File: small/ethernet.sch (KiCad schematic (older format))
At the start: 26 parts, among them J6 RJ45_Amphenol_RJMG1BD3B8K1ANR, U4 ENC28J60x-SS, Y1 Crystal

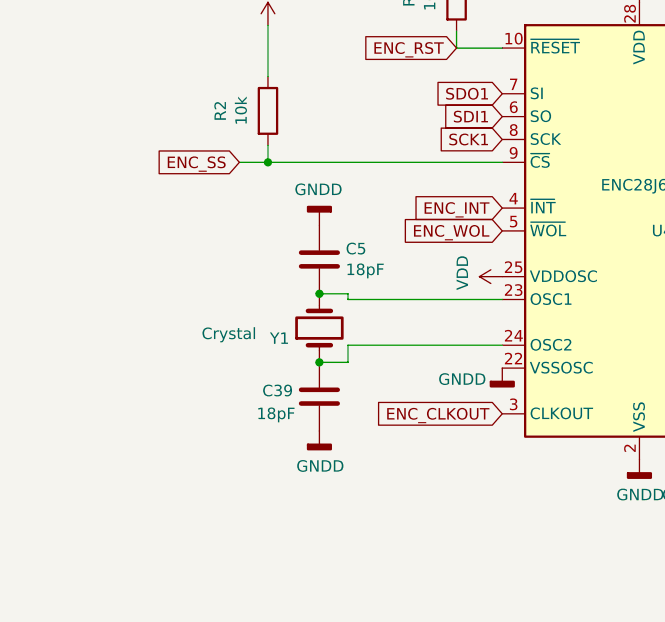
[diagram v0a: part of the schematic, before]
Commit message: oscillator footprint and capacitors changed
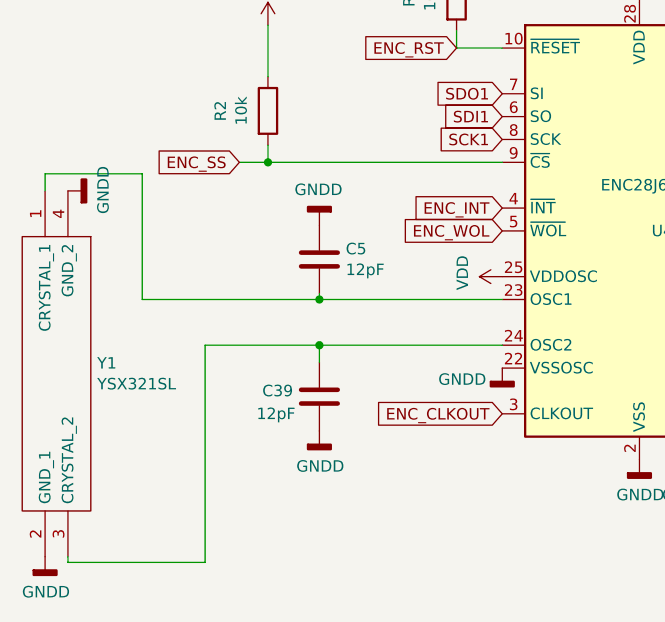
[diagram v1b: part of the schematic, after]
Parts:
- removed Y1: Crystal, Crystal:Crystal_SMD_3225-4Pin_3.2x2.5mm, symbol Device:Crystal
- added Y1: YSX321SL, small:YSX321SL, symbol YSX321SL:YSX321SL
- C39, C5: value 18pF -> 12pF; LCSC C1647 -> C38523; MPN CL10C180JB8NNNC -> CL10C120JB8NNNC
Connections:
- wire segments 76 -> 82
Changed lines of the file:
@@
 SDO1
-$Comp
-L Device:Crystal Y?
-U 1 1 60781A1A
-P 1850 3425
-AR Path="/60781A1A" Ref="Y?"  Part="1"
-AR Path="/60757620/60781A1A" Ref="Y1"  Part="1"
-F 0 "Y1" V 1804 3556 50  0000 L CNN
-F 1 "Crystal" V 1825 3700 50  0000 L CNN
-F 2 "Crystal:Crystal_SMD_3225-4Pin_3.2x2.5mm" H 1850 3425 50  0001 C CNN
-F 3 "https://datasheet.lcsc.com/szlcsc/Yangxing-Tech-X322525MOB4SI_C9006.pdf" H 1850 3425 50  0001 C CNN
-F 4 " C9006" V 1850 3425 50  0001 C CNN "LCSC"
-F 5 "X322525MOB4SI" H 1850 3425 50  0001 C CNN "MPN"
-F 6 "0" H 1850 3425 50  0001 C CNN "source"
-F 7 "0.0928" H 1850 3425 50  0001 C CNN "Price"
-	1    1850 3425
-	0    -1   -1   0
-$EndComp
-Wire Wire Line
-	2650 3300 1975 3300
-Wire Wire Line
-	1975 3300 1975 3275
-Wire Wire Line
-	1975 3275 1850 3275
-Wire Wire Line
-	2650 3500 1975 3500
-Wire Wire Line
-	1975 3500 1975 3575
-Wire Wire Line
-	1975 3575 1850 3575
 $Comp
 L Device:C C?
@@
 AR Path="/60757620/60781A26" Ref="C5"  Part="1"
 F 0 "C5" H 1965 3171 50  0000 L CNN
-F 1 "18pF" H 1965 3080 50  0000 L CNN
+F 1 "12pF" H 1965 3080 50  0000 L CNN
 F 2 "Capacitor_SMD:C_0603_1608Metric" H 1888 2975 50  0001 C CNN
-F 3 "https://datasheet.lcsc.com/szlcsc/Samsung-Electro-Mechanics-CL10C180JB8NNNC_C1647.pdf" H 1850 3125 50  0001 C CNN
-F 4 "C1647" H 1850 3125 50  0001 C CNN "LCSC"
-F 5 "CL10C180JB8NNNC" H 1850 3125 50  0001 C CNN "MPN"
+F 3 "https://datasheet.lcsc.com/szlcsc/Samsung-Electro-Mechanics-CL10C120JB8NNNC_C38523.pdf" H 1850 3125 50  0001 C CNN
+F 4 "C38523" H 1850 3125 50  0001 C CNN "LCSC"
+F 5 "CL10C120JB8NNNC" H 1850 3125 50  0001 C CNN "MPN"
 F 6 "0.0073" H 1850 3125 50  0001 C CNN "Price"
 F 7 "0" H 1850 3125 50  0001 C CNN "source"
@@
 	1    0    0    -1
 $EndComp
-Connection ~ 1850 3275
 $Comp
 L power:GNDD #PWR?
@@
 AR Path="/60757620/609672F4" Ref="C39"  Part="1"
 F 0 "C39" H 1600 3750 50  0000 L CNN
-F 1 "18pF" H 1575 3650 50  0000 L CNN
+F 1 "12pF" H 1575 3650 50  0000 L CNN
 F 2 "Capacitor_SMD:C_0603_1608Metric" H 1888 3575 50  0001 C CNN
-F 3 "https://datasheet.lcsc.com/szlcsc/Samsung-Electro-Mechanics-CL10C180JB8NNNC_C1647.pdf" H 1850 3725 50  0001 C CNN
-F 4 "C1647" H 1850 3725 50  0001 C CNN "LCSC"
-F 5 "CL10C180JB8NNNC" H 1850 3725 50  0001 C CNN "MPN"
+F 3 "https://datasheet.lcsc.com/szlcsc/Samsung-Electro-Mechanics-CL10C120JB8NNNC_C38523.pdf" H 1850 3725 50  0001 C CNN
+F 4 "C38523" H 1850 3725 50  0001 C CNN "LCSC"
+F 5 "CL10C120JB8NNNC" H 1850 3725 50  0001 C CNN "MPN"
 F 6 "0.0073" H 1850 3725 50  0001 C CNN "Price"
 F 7 "0" H 1850 3725 50  0001 C CNN "source"
@@
 	1    0    0    -1
 $EndComp
-Connection ~ 1850 3575
 Wire Wire Line
 	1500 2700 1625 2700
@@
 Text GLabel 1500 2700 0    50   Input ~ 0
 ENC_SS
+$Comp
+L YSX321SL:YSX321SL Y1
+U 1 1 603D57CF
+P 750 2825
+F 0 "Y1" V 1504 2953 50  0000 L CNN
+F 1 "YSX321SL" V 1595 2953 50  0000 L CNN
+F 2 "small:YSX321SL" H 2200 2925 50  0001 L CNN
+F 3 "https://datasheet.lcsc.com/szlcsc/YSX321SL-30MHZ-10PF-8PPM_C70576.pdf" H 2200 2825 50  0001 L CNN
+F 4 "Crystal" H 2200 2725 50  0001 L CNN "Description"
+F 5 "0.8" H 2200 2625 50  0001 L CNN "Height"
+F 6 "YXC" H 2200 2525 50  0001 L CNN "Manufacturer_Name"
+F 7 "YSX321SL" H 2200 2425 50  0001 L CNN "Manufacturer_Part_Number"
+F 8 "" H 2200 2325 50  0001 L CNN "Mouser Part Number"
+F 9 "" H 2200 2225 50  0001 L CNN "Mouser Price/Stock"
+F 10 "" H 2200 2125 50  0001 L CNN "Arrow Part Number"
+F 11 "" H 2200 2025 50  0001 L CNN "Arrow Price/Stock"
+	1    750  2825
+	0    1    1    0
+$EndComp
+Wire Wire Line
+	1850 3300 1850 3275
+Wire Wire Line
+	1850 3500 1850 3575
+Wire Wire Line
+	1850 3300 2650 3300
+Wire Wire Line
+	650  2825 650  2750
+Connection ~ 1850 3300
+Wire Wire Line
+	1075 3300 1075 2750
+Wire Wire Line
+	650  2750 1075 2750
+Wire Wire Line
+	1075 3300 1850 3300
+Wire Wire Line
+	750  4450 1350 4450
+Wire Wire Line
+	1350 4450 1350 3500
+Wire Wire Line
+	1350 3500 1850 3500
+Connection ~ 1850 3500
+Wire Wire Line
+	1850 3500 2650 3500
+Wire Wire Line
+	750  4425 750  4450
+$Comp
+L power:GNDD #PWR?
+U 1 1 603E3AD9
+P 650 4425
+AR Path="/603E3AD9" Ref="#PWR?"  Part="1"
+AR Path="/60757620/603E3AD9" Ref="#PWR0192"  Part="1"
+F 0 "#PWR0192" H 650 4175 50  0001 C CNN
+F 1 "GNDD" H 654 4270 50  0000 C CNN
+F 2 "" H 650 4425 50  0001 C CNN
+F 3 "" H 650 4425 50  0001 C CNN
+	1    650  4425
+	1    0    0    -1
+$EndComp
+$Comp
+L power:GNDD #PWR?
+U 1 1 603E5CE0
+P 750 2825
+AR Path="/603E5CE0" Ref="#PWR?"  Part="1"
+AR Path="/60757620/603E5CE0" Ref="#PWR0193"  Part="1"
+F 0 "#PWR0193" H 750 2575 50  0001 C CNN
+F 1 "GNDD" H 754 2670 50  0000 C CNN
+F 2 "" H 750 2825 50  0001 C CNN
+F 3 "" H 750 2825 50  0001 C CNN
+	1    750  2825
+	0    -1   -1   0
+$EndComp
 $EndSCHEMATC

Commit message: 25 MHZ crystal part added.
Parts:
- Y1: LCSC (none) -> C9006
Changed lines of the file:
@@
 F 10 "" H 2200 2125 50  0001 L CNN "Arrow Part Number"
 F 11 "" H 2200 2025 50  0001 L CNN "Arrow Price/Stock"
+F 12 "C9006" V 750 2825 50  0001 C CNN "LCSC"
 	1    750  2825
 	0    1    1    0
